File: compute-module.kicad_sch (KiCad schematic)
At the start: 13 parts, among them J7 DF40HC(3.0)-100DS-0.4v, J8 DF40HC(3.0)-100DS-0.4v, M1 compute-module-4-1.5mm, Q6 BSS138-7-F

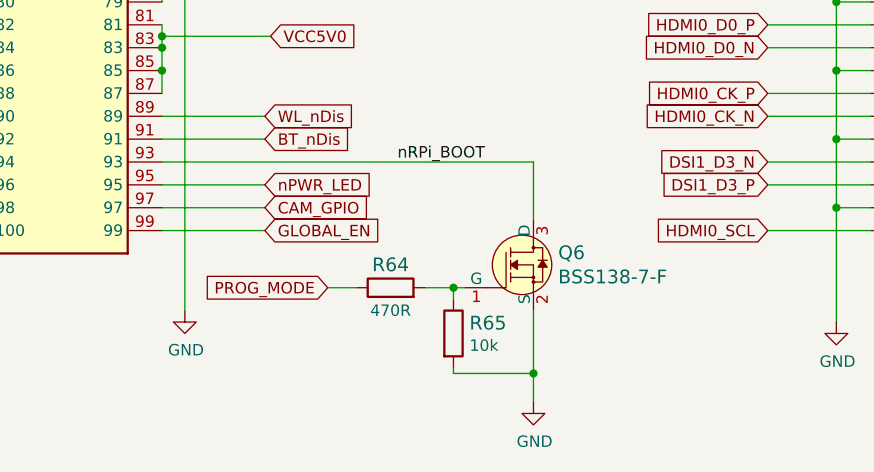
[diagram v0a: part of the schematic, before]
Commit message: Update Q6 symbol and footprint
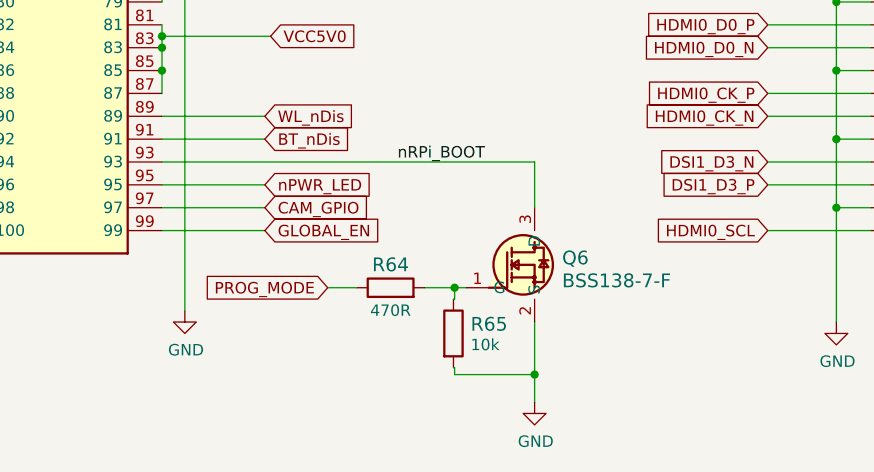
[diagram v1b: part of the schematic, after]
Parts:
- Q6: footprint scalenode-cm4-baseboard-footprints:SOT-23-3 -> antmicro-footprints:SOT-23-3; symbol scalenode-cm4-baseboard:BSS138-7-F -> antmicroTransistorsFETsMOSFETsSingle:BSS138-7-F; Author (none) -> Antmicro; License (none) -> Apache-2.0

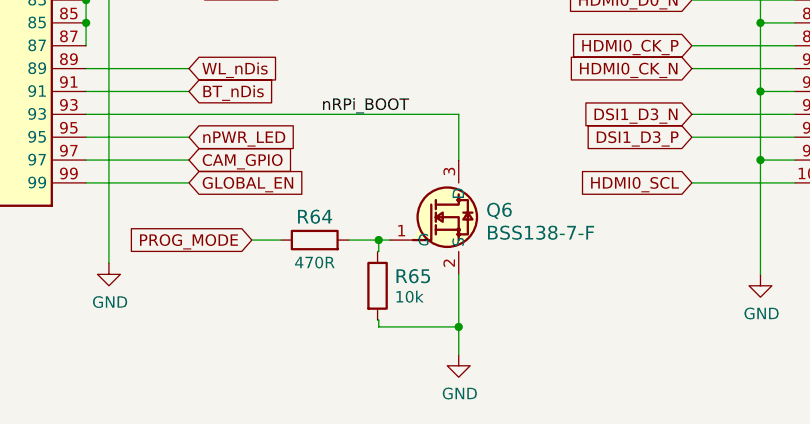
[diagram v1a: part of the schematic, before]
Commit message: Update R5, R9, R10, R11, R12, R13, R14, R19, R55, R65 symbol and footprint
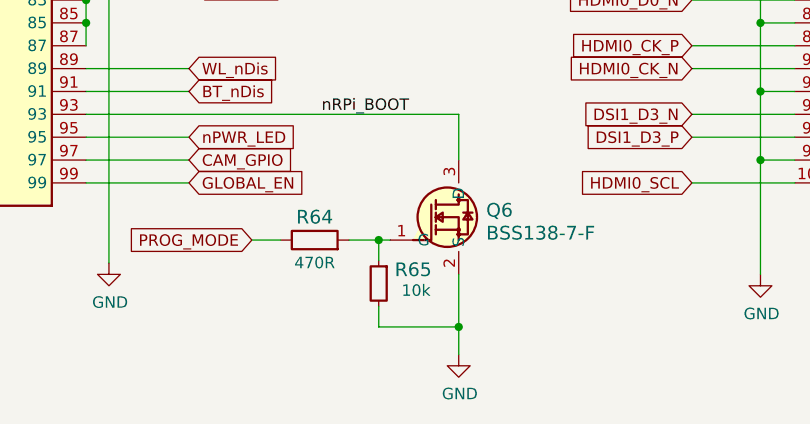
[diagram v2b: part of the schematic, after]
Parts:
- R65: footprint scalenode-cm4-baseboard-footprints:0402-res -> antmicro-footprints:R_0402_1005Metric; symbol scalenode-cm4-baseboard:R_10k_0402 -> antmicroResistors0402:R_10k_0402; Author (none) -> Antmicro; License (none) -> Apache-2.0; MPN CRCW040210K0FKEDHP -> CR0402-FX-1002GLF; Manufacturer VISHAY -> Bourns; Tolerance (none) -> 1%

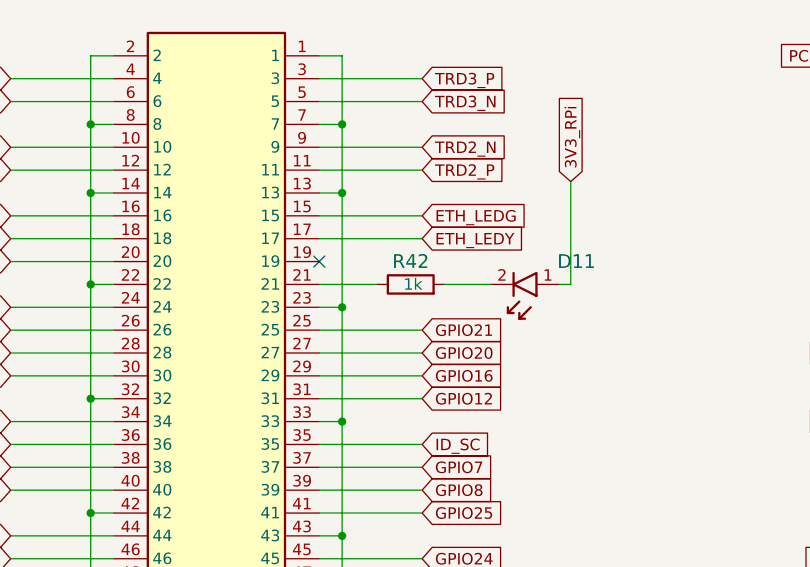
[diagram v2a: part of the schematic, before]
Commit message: Update R42 symbol and footprint
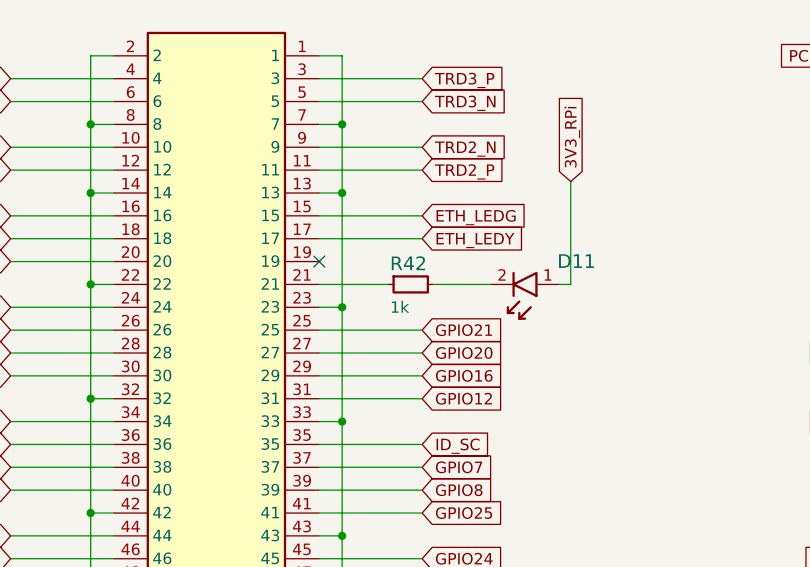
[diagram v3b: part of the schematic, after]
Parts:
- R42: footprint scalenode-cm4-baseboard-footprints:0603-res -> antmicro-footprints:R_0603_1608Metric; symbol scalenode-cm4-baseboard:R_1k_0603 -> antmicroResistors0603:R_1k_0603; Author (none) -> Antmicro; License (none) -> Apache-2.0; MPN CR0603-JW-102ELF -> CR0603-FX-1001ELF; Manufacturer BOURNS -> Bourns; Tolerance (none) -> 1%

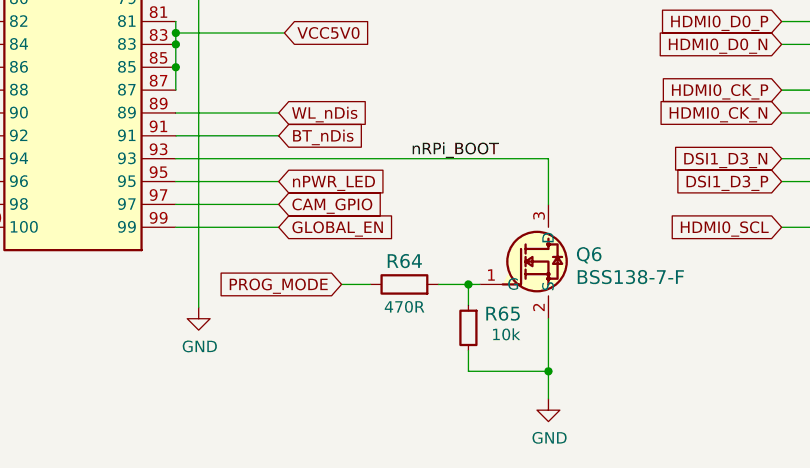
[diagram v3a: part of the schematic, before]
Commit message: Update R64 symbol and footprint
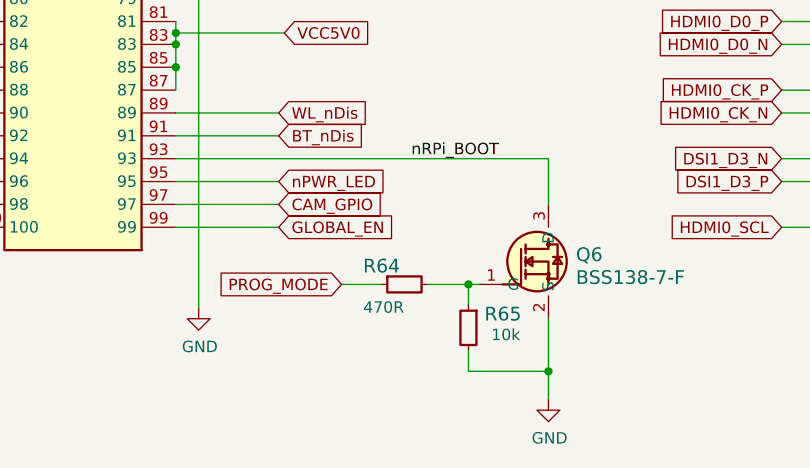
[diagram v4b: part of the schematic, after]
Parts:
- R64: footprint scalenode-cm4-baseboard-footprints:0402-res -> antmicro-footprints:R_0402_1005Metric; symbol scalenode-cm4-baseboard:R_470R_0402 -> antmicroResistors0402:R_470R_0402; Author (none) -> Antmicro; License (none) -> Apache-2.0; MPN CRCW0402470RFKED -> CR0402-FX-4700GLF; Manufacturer VISHAY -> Bourns; Tolerance (none) -> 1%

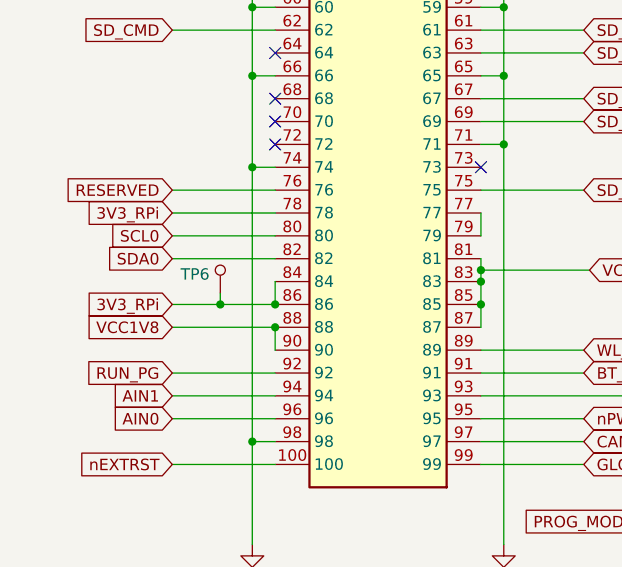
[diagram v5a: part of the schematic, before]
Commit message: Update TP2, TP3, TP4, TP5, TP6, TP7 symbol and footprint
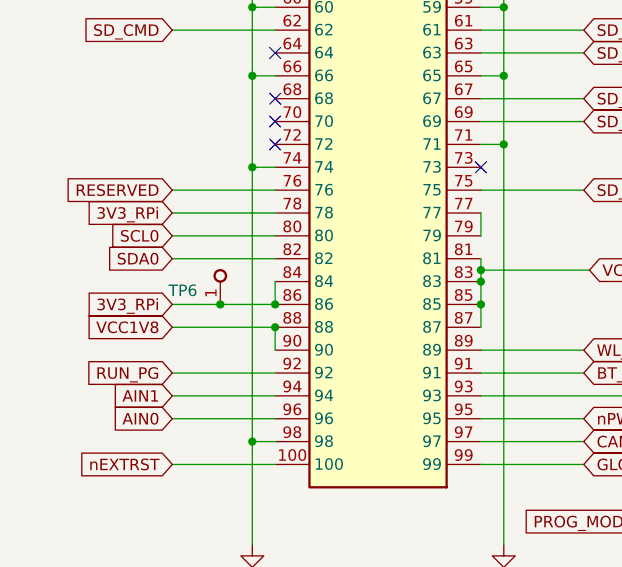
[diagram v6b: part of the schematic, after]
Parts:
- TP6: footprint scalenode-cm4-baseboard-footprints:Testpoint_smd_1mm -> antmicro-footprints:Testpoint_smd_1mm; symbol scalenode-cm4-baseboard:TP_SMD1MM -> antmicroTestPoints:TP_1mm_SMD; Author (none) -> Antmicro; License (none) -> Apache-2.0

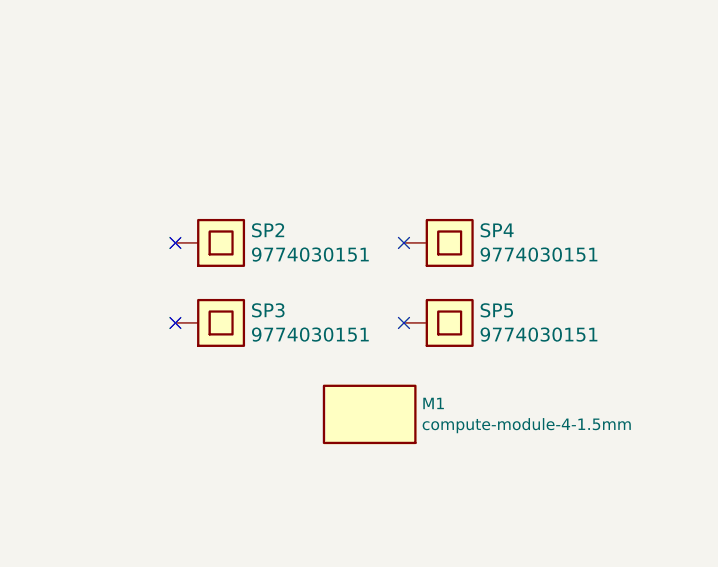
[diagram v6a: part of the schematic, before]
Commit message: Update SP2, SP3, SP4, SP5 symbol and footprint
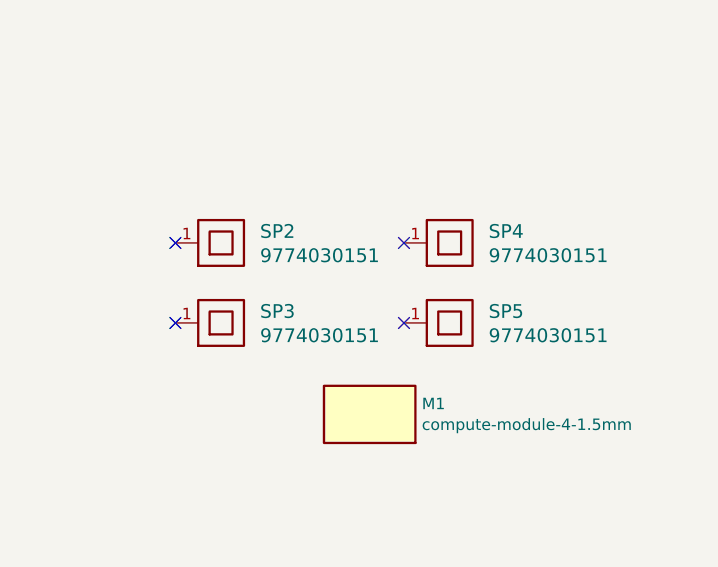
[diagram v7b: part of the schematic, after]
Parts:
- SP2, SP3, SP4, SP5: footprint scalenode-cm4-baseboard-footprints:9774030151 -> antmicro-footprints:9774030151; symbol scalenode-cm4-baseboard:9774030151 -> antmicroMechanicalParts:9774030151; Author (none) -> Antmicro; License (none) -> Apache-2.0; Manufacturer Wurth Elektronik -> Würth Elektronik
